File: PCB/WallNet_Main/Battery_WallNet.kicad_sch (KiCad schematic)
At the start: 20 parts, among them J2 USB_C_Receptacle_PowerOnly_6P, J3 Conn_01x04_Pin, U3 BQ25895RTWT

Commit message: bruh
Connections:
- net SYS renamed VDD_nrf
- net VDD_nrf: no longer D4.2 (A), R7.1, R8.1, R9.1
- new net VDD_nRF: D4.2 (A), R7.1, R8.1, R9.1
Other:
- note added: "Inputs/Outputs"
- moved on the sheet: C10, C4, C5, C6, C7, C8, C9, D4, L1, R4, R5, R6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

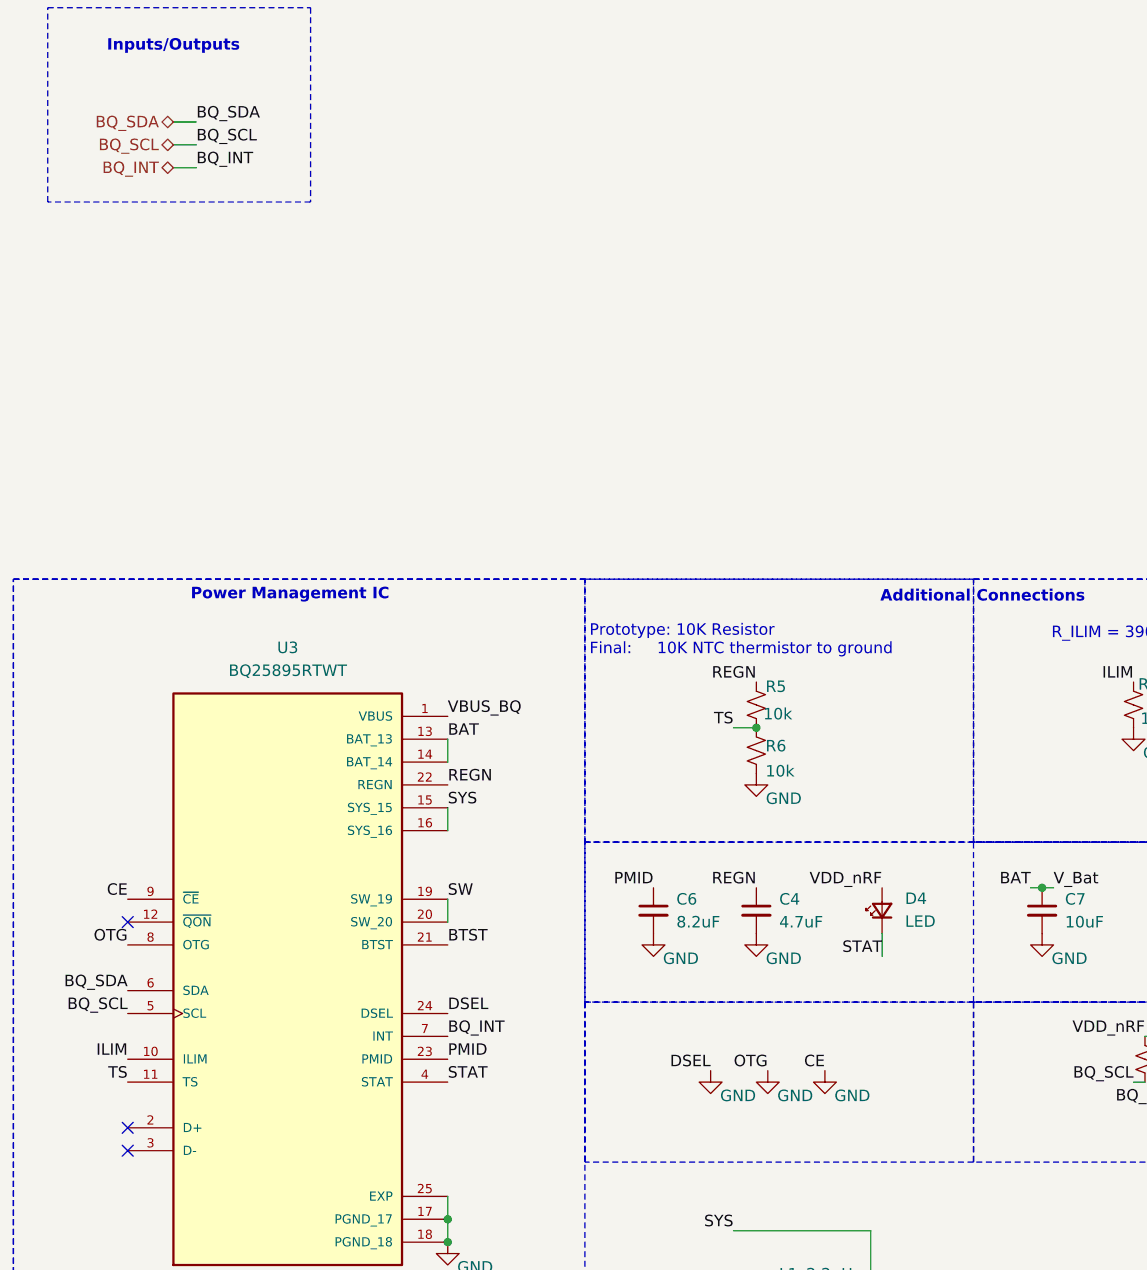
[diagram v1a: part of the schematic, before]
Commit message: Changed some Heir connections
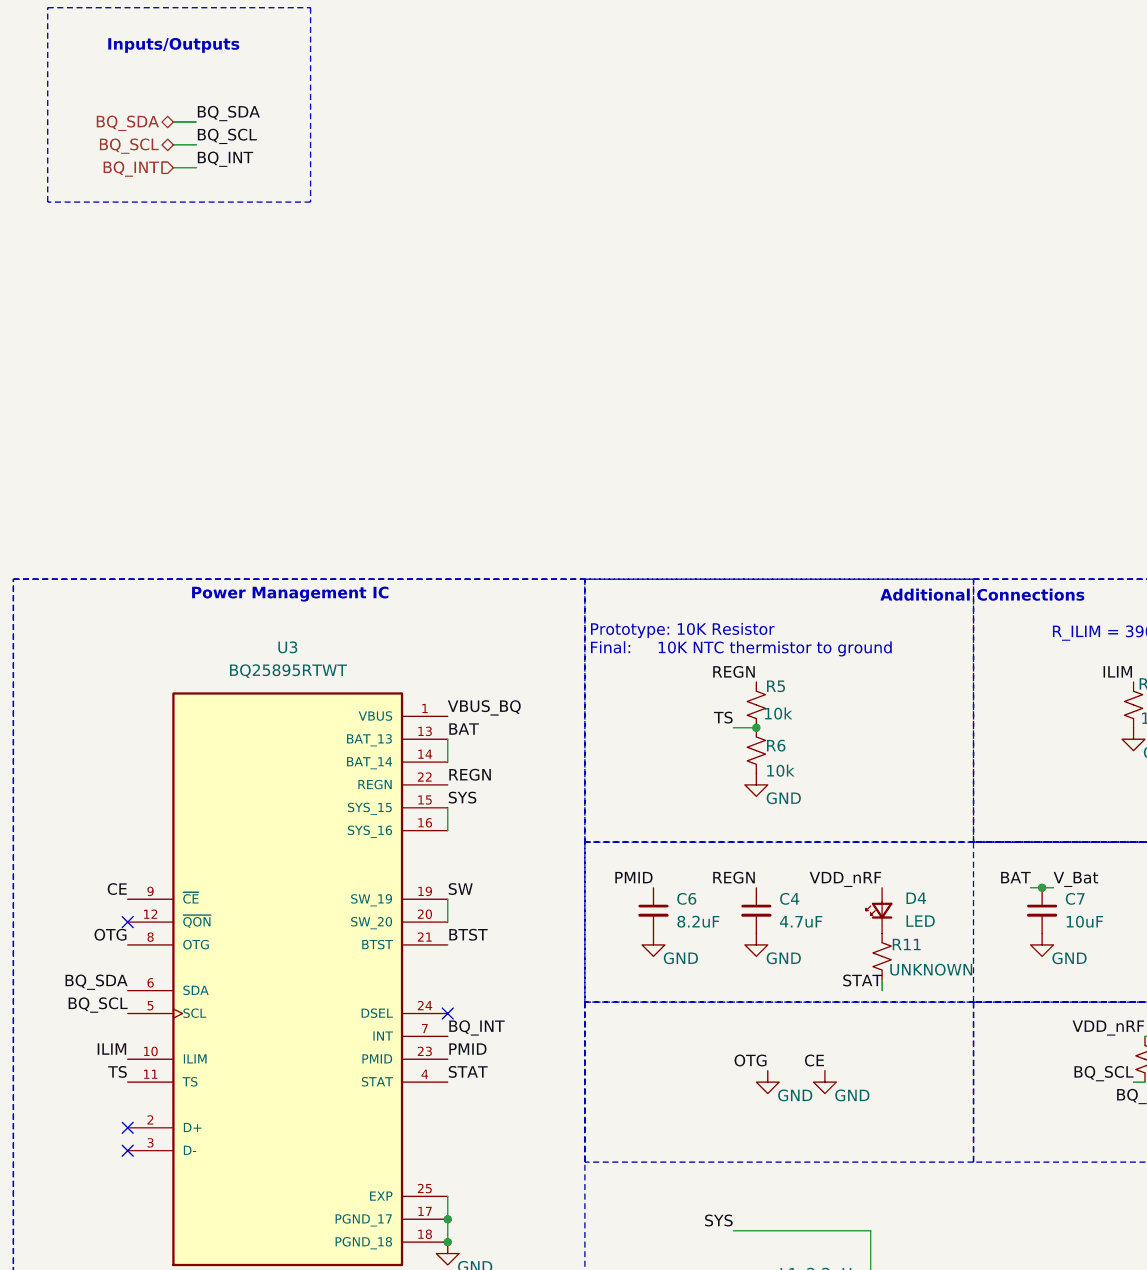
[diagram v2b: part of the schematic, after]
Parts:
- added R11: UNKNOWN, symbol Device:R_Small_US
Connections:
- net GND: no longer U3.24 (DSEL)
- net STAT: now also R11.2; no longer D4.1 (K)
- new net: D4.1 (K), R11.1
- no-connect marks 3 -> 4
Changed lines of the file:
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@@
 	)
 	(no_connect
+		(at 71.12 125.73)
+	)
+	(no_connect
 		(at 35.56 140.97)
 	)
@@
 	(wire
 		(pts
+			(xy 119.38 123.19) (xy 119.38 121.92)
+		)
+		(stroke
+			(width 0)
+			(type default)
+		)
+	)
+	(wire
+		(pts
 			(xy 102.87 149.86) (xy 118.11 149.86)
 		)
@@
 	(wire
 		(pts
-			(xy 119.38 119.38) (xy 119.38 116.84)
-		)
-		(stroke
-			(width 0)
-			(type default)
-		)
-	)
-	(wire
-		(pts
 			(xy 123.19 156.21) (xy 132.08 156.21)
 		)
@@
 		)
 	)
-	(label "DSEL"
-		(at 71.12 125.73 0)
-		(effects
-			(font
-				(size 1.27 1.27)
-			)
-			(justify left bottom)
-		)
-	)
 	(label "V_Bat"
 		(at 199.39 39.37 0)
@@
 		)
 	)
-	(label "DSEL"
-		(at 100.33 132.08 180)
-		(effects
-			(font
-				(size 1.27 1.27)
-			)
-			(justify right bottom)
-		)
-	)
 	(label "CE"
 		(at 113.03 132.08 180)
@@
 	)
 	(label "STAT"
-		(at 119.38 119.38 180)
+		(at 119.38 123.19 180)
 		(effects
 			(font
@@
 	)
 	(hierarchical_label "BQ_INT"
-		(shape bidirectional)
+		(shape input)
 		(at 40.64 31.75 180)
 		(effects
@@
 	)
 	(symbol
+		(lib_id "Device:R_Small_US")
+		(at 119.38 119.38 0)
+		(unit 1)
+		(exclude_from_sim no)
+		(in_bom yes)
+		(on_board yes)
+		(dnp no)
+		(property "Reference" "R11"
+			(at 120.396 118.11 0)
+			(effects
+				(font
+					(size 1.27 1.27)
+				)
+				(justify left)
+			)
+		)
+		(property "Value" "UNKNOWN"
+			(at 120.142 120.904 0)
+			(effects
+				(font
+					(size 1.27 1.27)
+				)
+				(justify left)
+			)
+		)
+		(property "Footprint" ""
+			(at 119.38 119.38 0)
+			(effects
+				(font
+					(size 1.27 1.27)
+				)
+				(hide yes)
+			)
+		)
+		(property "Datasheet" "~"
+			(at 119.38 119.38 0)
+			(effects
+				(font
+					(size 1.27 1.27)
+				)
+				(hide yes)
+			)
+		)
+		(property "Description" "Resistor, small US symbol"
+			(at 119.38 119.38 0)
+			(effects
+				(font
+					(size 1.27 1.27)
+				)
+				(hide yes)
+			)
+		)
+		(pin "1"
+		)
+		(pin "2"
+		)
+		(instances
+			(project "WallNet_Main"
+				(path "/3272dd14-9e34-4275-b10b-c06dab1b3ca1/ac25aec4-60b5-4d7f-9f99-a074eef21076"
+					(reference "R11")
+					(unit 1)
+				)
+			)
+		)
+	)
+	(symbol
 		(lib_id "power:GND")
 		(at 71.12 151.13 0)
@@
 					(unit 1)
 				)
-			)
-		)
-	)
-	(symbol
-		(lib_id "power:GND")
-		(at 100.33 132.08 0)
-		(unit 1)
-		(exclude_from_sim no)
-		(in_bom yes)
-		(on_board yes)
-		(dnp no)
-		(property "Reference" "#PWR06"
-			(at 100.33 138.43 0)
-			(effects
-				(font
-					(size 1.27 1.27)
-				)
-				(hide yes)
-			)
-		)
-		(property "Value" "GND"
-			(at 103.378 134.874 0)
-			(effects
-				(font
-					(size 1.27 1.27)
-				)
-			)
-		)
-		(property "Footprint" ""
-			(at 100.33 132.08 0)
-			(effects
-				(font
-					(size 1.27 1.27)
-				)
-				(hide yes)
-			)
-		)
-		(property "Datasheet" ""
-			(at 100.33 132.08 0)
-			(effects
-				(font
-					(size 1.27 1.27)
-				)
-				(hide yes)
-			)
-		)
-		(property "Description" "Power symbol creates a global label with name \"GND\" , ground"
-			(at 100.33 132.08 0)
-			(effects
-				(font
-					(size 1.27 1.27)
-				)
-				(hide yes)
-			)
-		)
-		(pin "1"
-		)
-		(instances
-			(project "WallNet_Main"
-				(path "/3272dd14-9e34-4275-b10b-c06dab1b3ca1/ac25aec4-60b5-4d7f-9f99-a074eef21076"
-					(reference "#PWR06")
-					(unit 1)
-				)

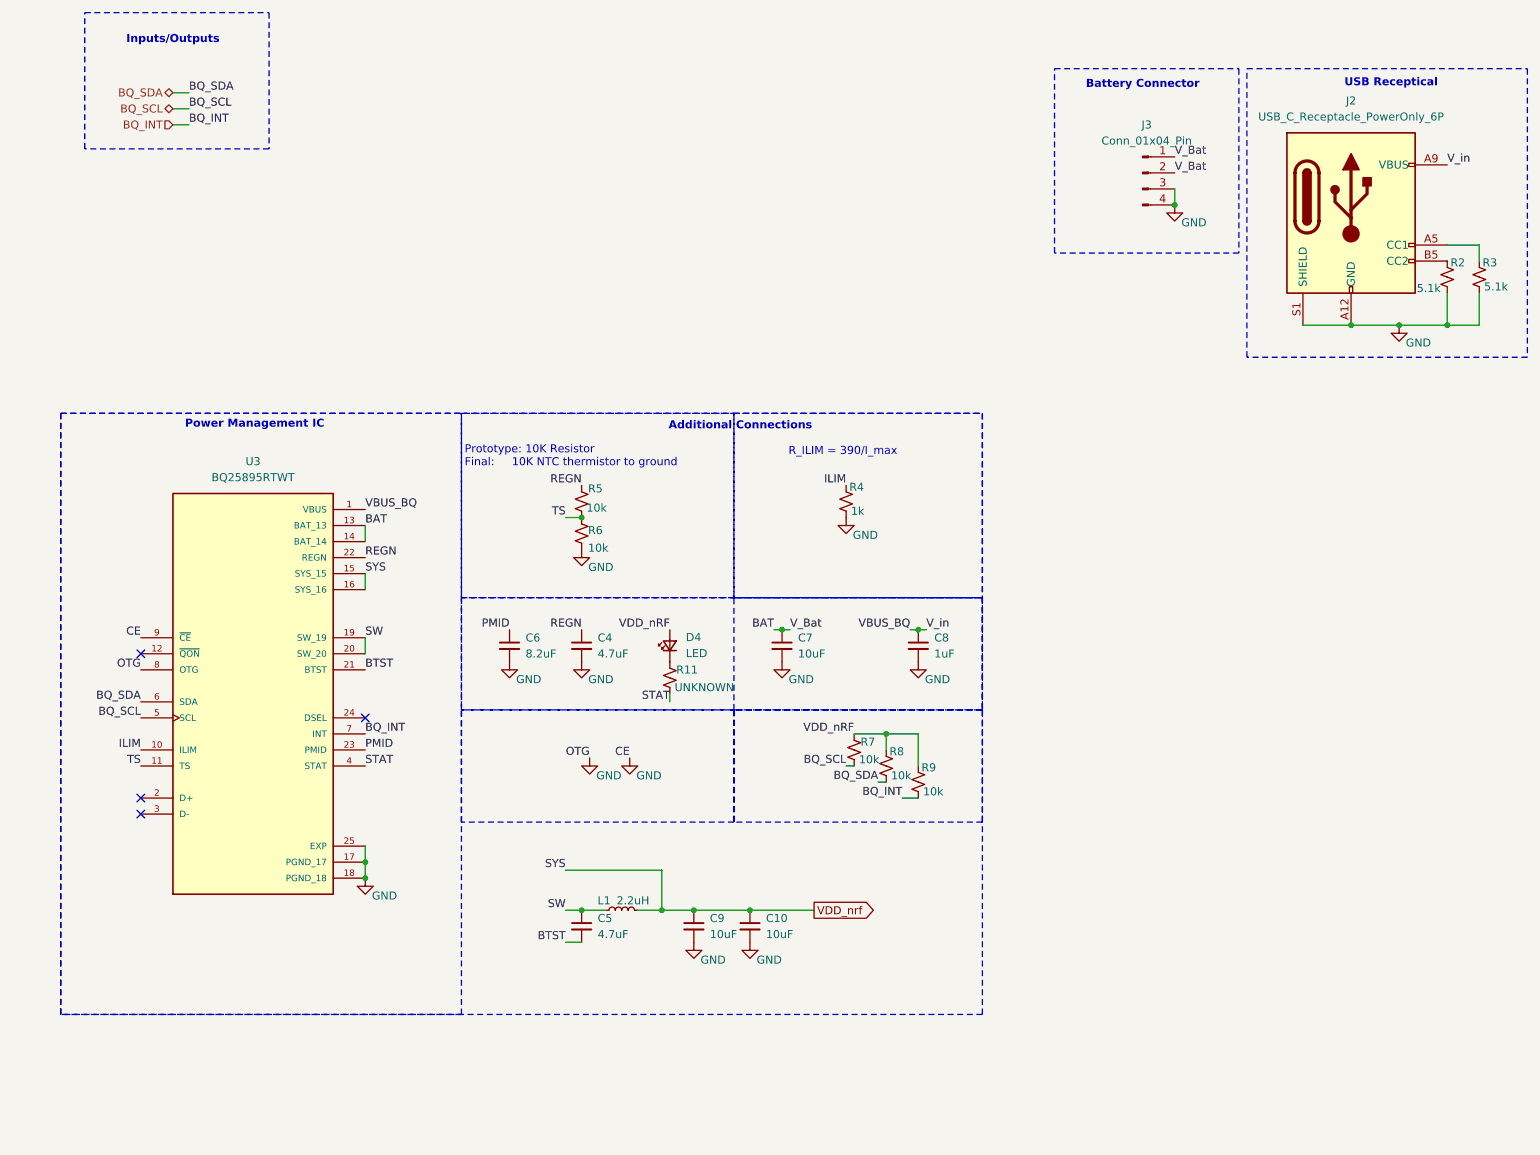
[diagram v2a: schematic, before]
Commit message: E-ink & GPS connection Complete
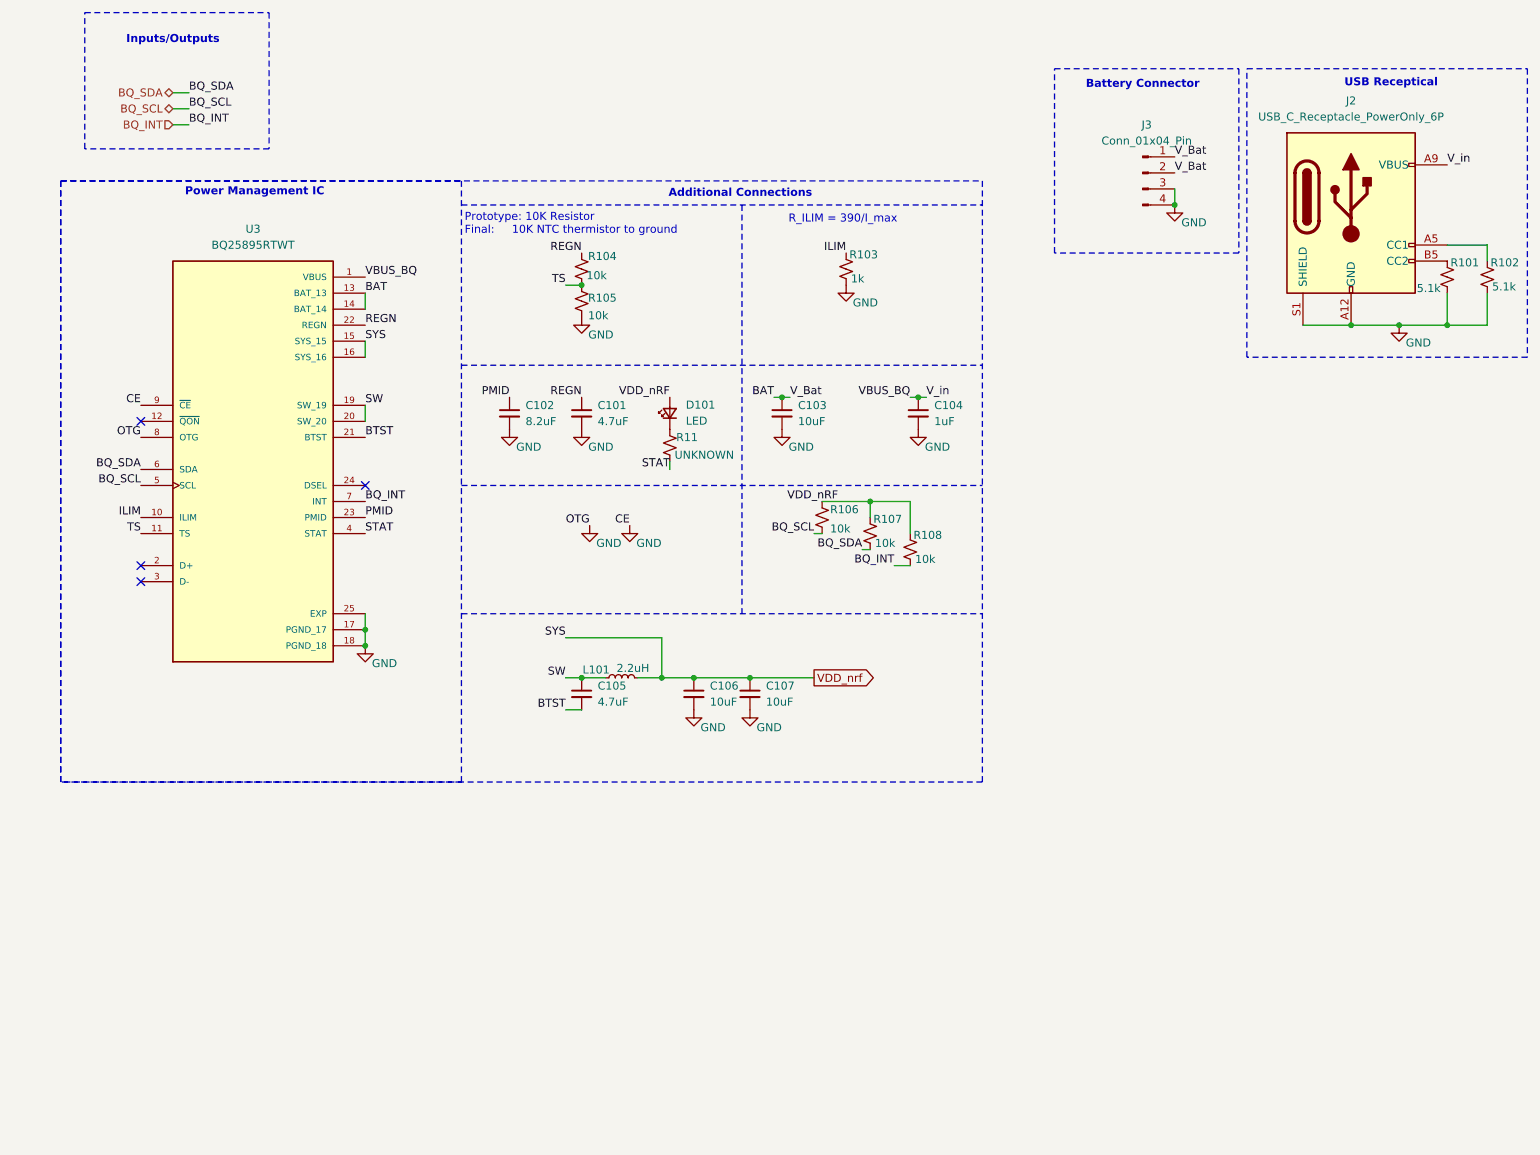
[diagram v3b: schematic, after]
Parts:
- renumbered C4 to C101, C6 to C102, C7 to C103, C8 to C104, C5 to C105, C9 to C106, C10 to C107, D4 to D101, L1 to L101, R2 to R101, R3 to R102, R4 to R103, R5 to R104, R6 to R105, R7 to R106, R8 to R107, R9 to R108
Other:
- moved on the sheet: C101, C102, C103, C104, C105, C106, C107, D101, L101, R102, R103, R104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
